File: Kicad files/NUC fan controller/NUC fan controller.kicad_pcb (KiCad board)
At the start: 2 copper layers, 14 parts, among them J1 M5Atom left, J2 M5Atom right, J3 sensor 1 connector, J4 sensor 2 connector, J5 sensor 3 connector, J6 Fan 1, J7 Fan 2, J8 Fan 3, J9 Fan 4

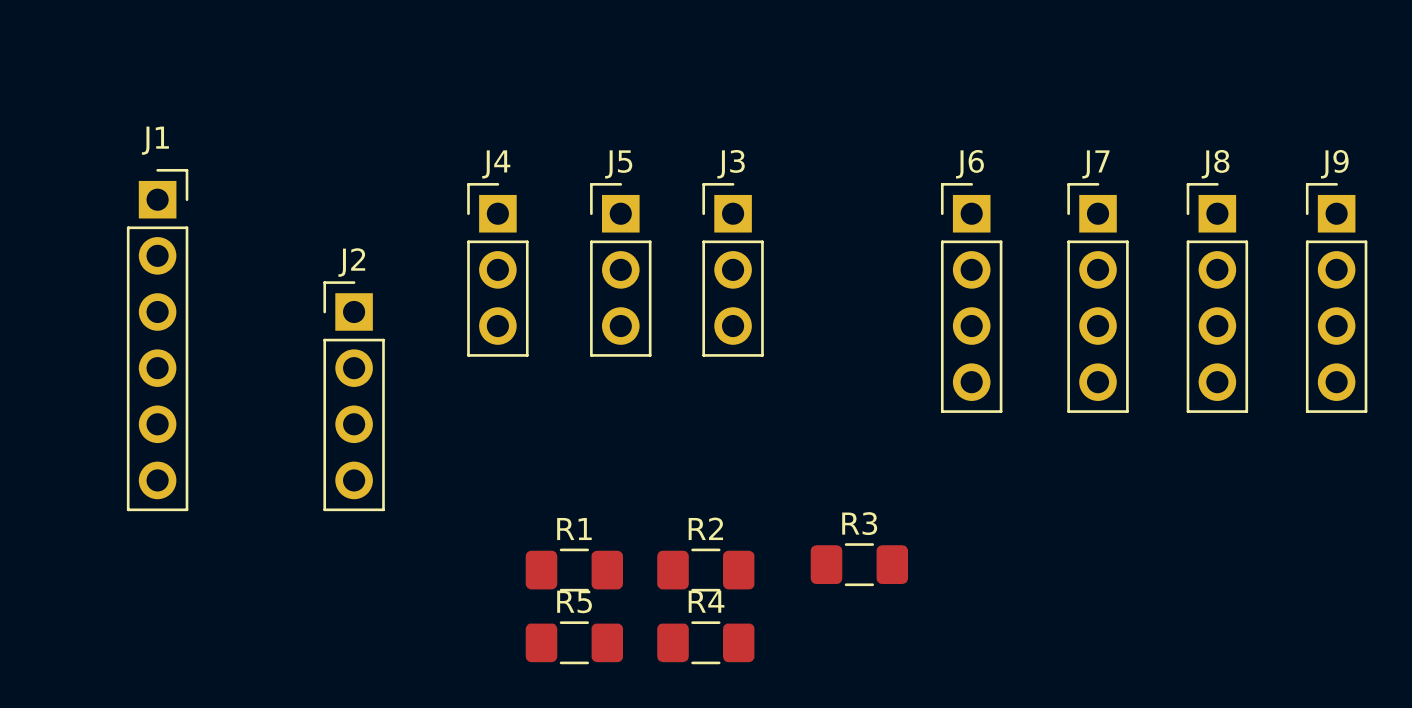
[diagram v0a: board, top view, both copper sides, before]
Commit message: Added software pullup on tacho pin. (less resistors needed)
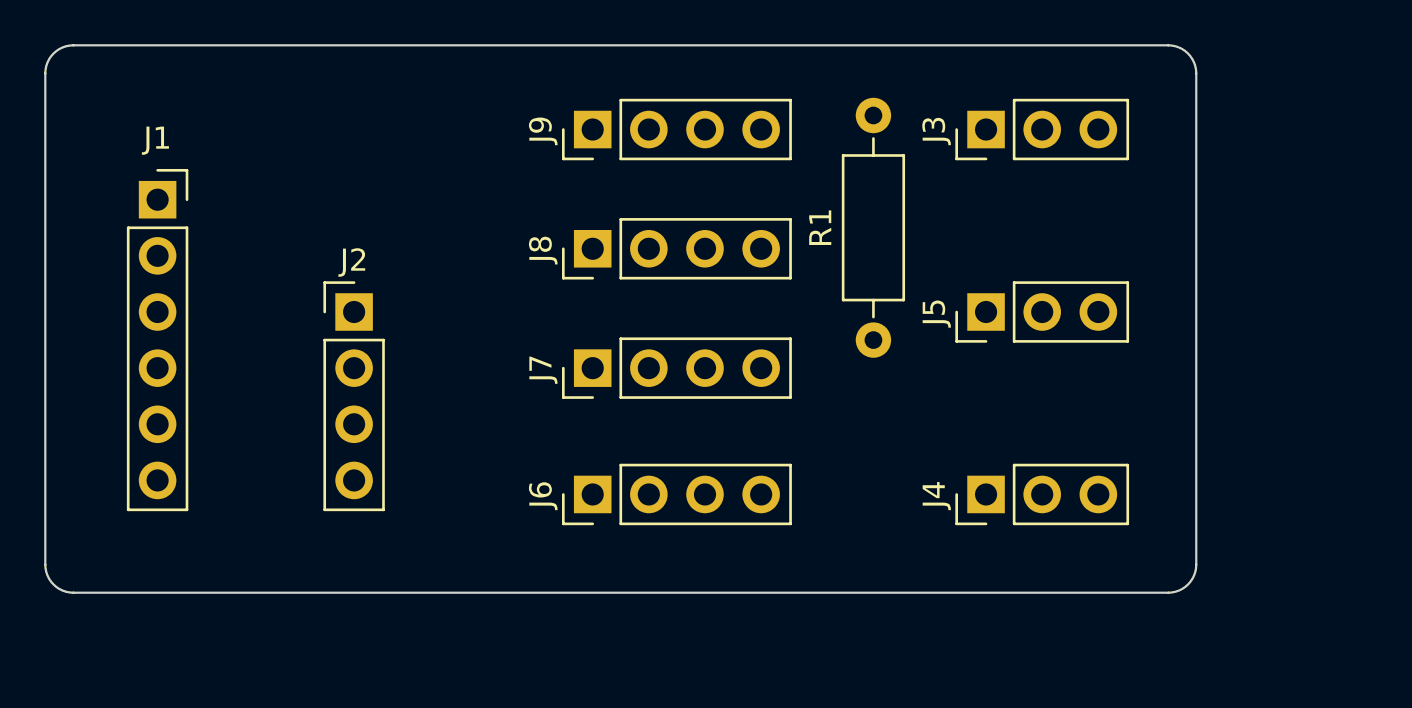
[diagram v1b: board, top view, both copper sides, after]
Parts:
- removed R2, R3, R4, R5: 4.7k, Resistor_SMD:R_1206_3216Metric_Pad1.42x1.75mm_HandSolder
- R1: footprint Resistor_SMD:R_1206_3216Metric_Pad1.42x1.75mm_HandSolder -> Resistor_THT:R_Axial_DIN0207_L6.3mm_D2.5mm_P10.16mm_Horizontal
- moved J9 33.9 mm to (113.7, 64.1), turned to 90 degrees
- moved J8 28.3 mm to (113.7, 69.5), turned to 90 degrees
- moved J4 25.5 mm to (131.5, 80.6), turned to 90 degrees
- moved J7 23.9 mm to (113.7, 74.9), turned to 90 degrees
- moved J6 21.3 mm to (113.7, 80.6), turned to 90 degrees
- moved J5 17.1 mm to (131.5, 72.4), turned to 90 degrees
- moved R1 17.1 mm to (126.4, 73.7), turned to 90 degrees
- moved J3 12.1 mm to (131.5, 64.1), turned to 90 degrees
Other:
- board outline added: 52.1 x 24.8 mm
